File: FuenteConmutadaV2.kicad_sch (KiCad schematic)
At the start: 28 parts, among them J1 Conn_01x01_Pin, J2 Conn_01x01_Pin, J4 Conn_01x01_Pin, J5 USB_C_Receptacle_USB2.0

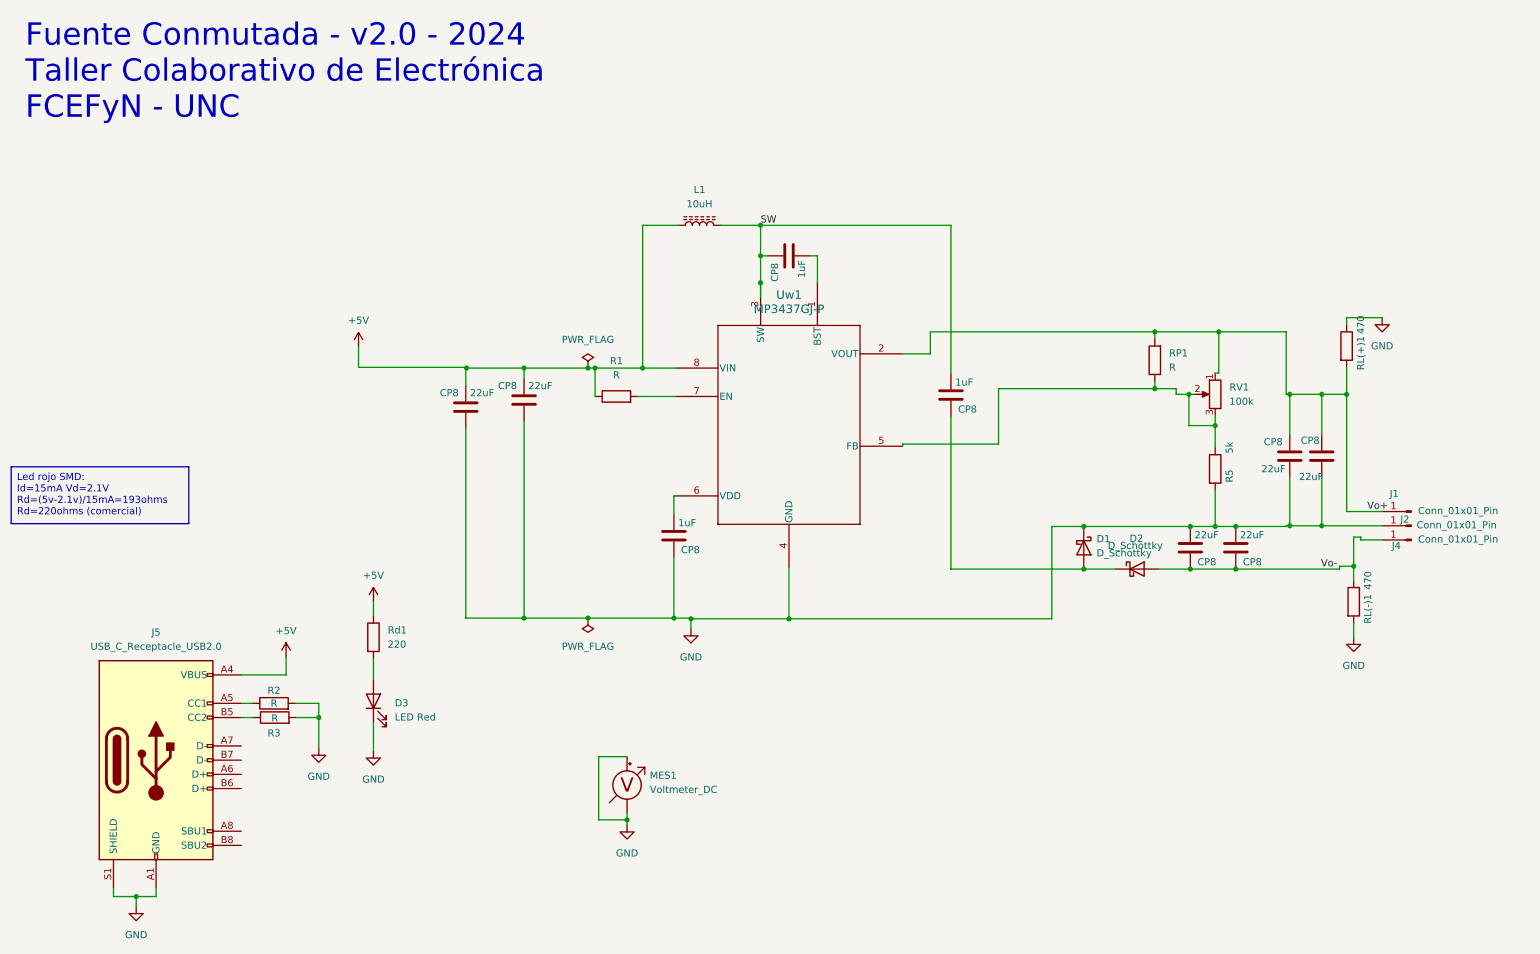
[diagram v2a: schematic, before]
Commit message: Cambios+pad banana
Pad banana diseñado
ajuste te tamaño de placa 80x40mm
ajuste vias
+mounting holes
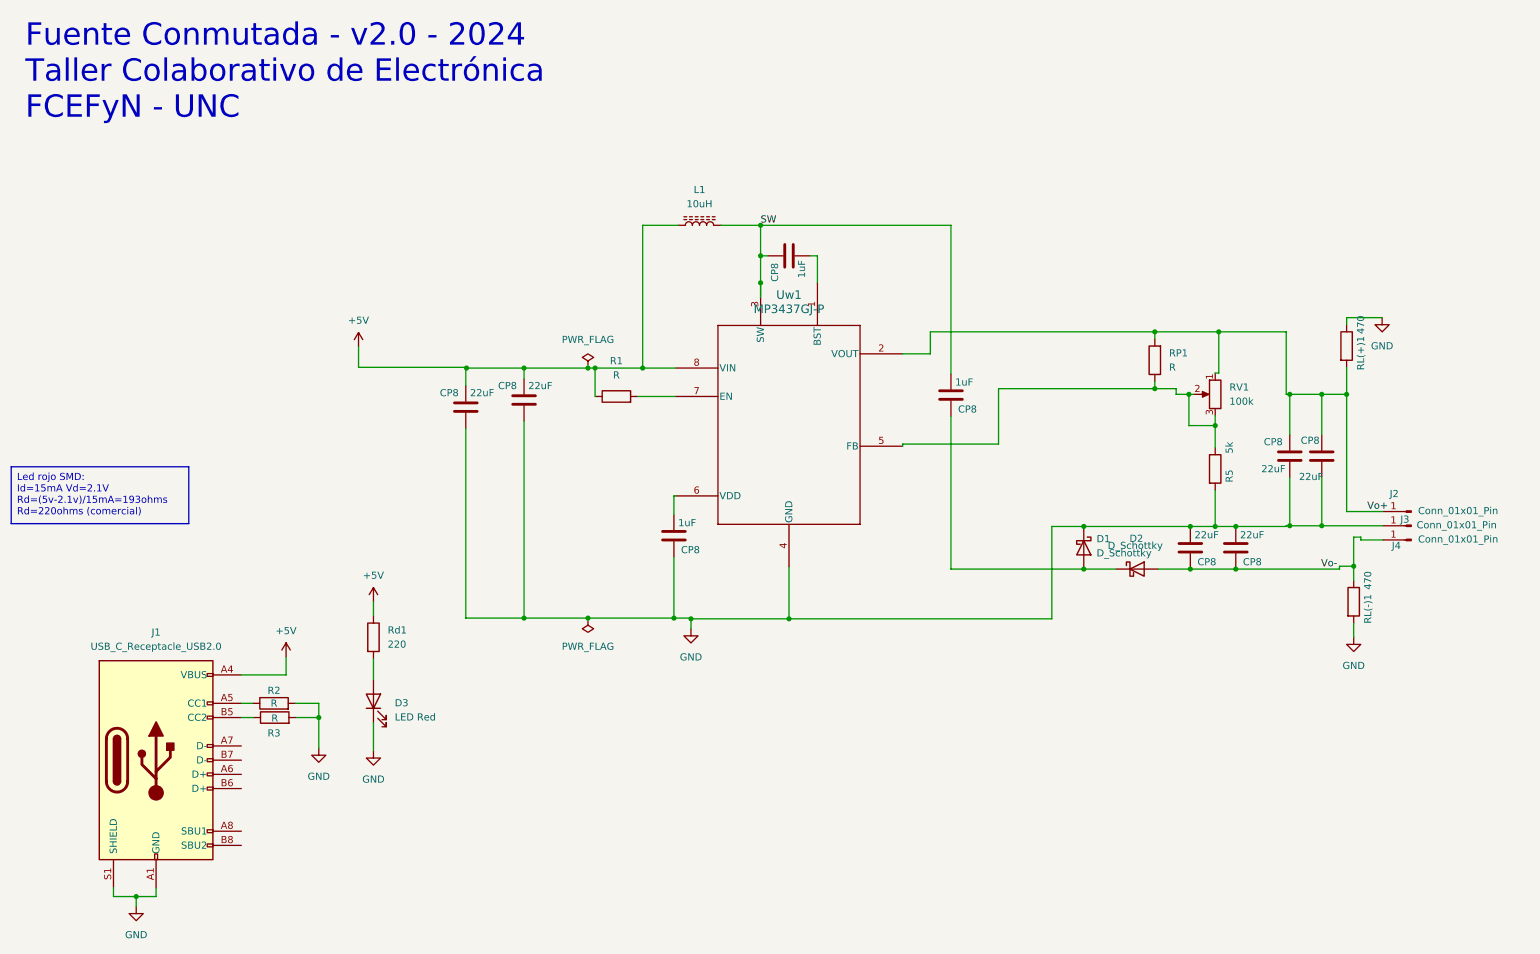
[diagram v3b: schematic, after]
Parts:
- removed MES1: Voltmeter_DC, Voltmeter:PRT-14313, symbol Device:Voltmeter_DC
- J2: renamed from J1; footprint Connector:CalTest_CT3151 -> Banana_elemon:Banana_209_elemon
- J3: renamed from J2; footprint Connector:CalTest_CT3151 -> Banana_elemon:Banana_209_elemon
- J4: footprint Connector:CalTest_CT3151 -> Banana_elemon:Banana_209_elemon
- renumbered J5 to J1
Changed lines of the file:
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@@
 	)
 	(junction
-		(at 124.079 159.639)
-		(diameter 0)
-		(color 0 0 0 0)
-	)
-	(junction
 		(at 95.377 78.867)
 		(diameter 0)
@@
 	(wire
 		(pts
-			(xy 124.079 148.336) (xy 118.999 148.336)
-		)
-		(stroke
-			(width 0)
-			(type default)
-		)
-	)
-	(wire
-		(pts
 			(xy 156.845 58.801) (xy 158.115 58.801)
 		)
@@
 	(wire
 		(pts
-			(xy 118.999 159.639) (xy 124.079 159.639)
-		)
-		(stroke
-			(width 0)
-			(type default)
-		)
-	)
-	(wire
-		(pts
 			(xy 78.74 120.65) (xy 78.74 123.19)
 		)
@@
 	(wire
 		(pts
-			(xy 124.079 159.639) (xy 124.079 160.528)
-		)
-		(stroke
-			(width 0)
-			(type default)
-		)
-	)
-	(wire
-		(pts
 			(xy 173.355 92.456) (xy 173.355 92.837)
 		)
@@
 	(wire
 		(pts
-			(xy 118.999 148.336) (xy 118.999 159.639)
-		)
-		(stroke
-			(width 0)
-			(type default)
-		)
-	)
-	(wire
-		(pts
 			(xy 229.235 89.154) (xy 229.235 93.091)
 		)
@@
 	(wire
 		(pts
-			(xy 124.079 158.496) (xy 124.079 159.639)
-		)
-		(stroke
-			(width 0)
-			(type default)
-		)
-	)
-	(wire
-		(pts
 			(xy 32.258 173.355) (xy 36.322 173.355)
 		)
@@
 	(symbol
 		(lib_id "power:GND")
-		(at 124.079 160.528 0)
-		(unit 1)
-		(exclude_from_sim no)
-		(in_bom yes)
-		(on_board yes)
-		(dnp no)
-		(fields_autoplaced yes)
-		(property "Reference" "#PWR06"
-			(at 124.079 166.878 0)
-			(effects
-				(font
-					(size 1.27 1.27)
-				)
-				(hide yes)
-			)
-		)
-		(property "Value" "GND"
-			(at 124.079 165.608 0)
-			(effects
-				(font
-					(size 1.27 1.27)
-				)
-			)
-		)
-		(property "Footprint" ""
-			(at 124.079 160.528 0)
-			(effects
-				(font
-					(size 1.27 1.27)
-				)
-				(hide yes)
-			)
-		)
-		(property "Datasheet" ""
-			(at 124.079 160.528 0)
-			(effects
-				(font
-					(size 1.27 1.27)
-				)
-				(hide yes)
-			)
-		)
-		(property "Description" ""
-			(at 124.079 160.528 0)
-			(effects
-				(font
-					(size 1.27 1.27)
-				)
-				(hide yes)
-			)
-		)
-		(pin "1"
-		)
-		(instances
-			(project "FuenteConmutadaV2"
-				(path "/d69a48d3-cc9a-476a-8449-ca4ce55f09c5"
-					(reference "#PWR06")
-					(unit 1)
-				)
-			)
-			(project "FuenteConmutada"
-				(path "/d7444c1b-87b0-4ff7-a57a-a32071ba4b64"
-					(reference "#PWR01")
-					(unit 1)
-				)
-			)
-		)
-	)
-	(symbol
-		(lib_id "power:GND")
 		(at 259.08 69.85 0)
 		(unit 1)
@@
 		(on_board yes)
 		(dnp no)
-		(property "Reference" "J2"
+		(property "Reference" "J3"
 			(at 263.144 105.918 0)
 			(effects
@@
 			)
 		)
-		(property "Footprint" "Connector:CalTest_CT3151"
-			(at 264.287 107.061 0)
+		(property "Footprint" "Banana_elemon:Banana_209_elemon"
+			(at 272.796 98.044 0)
 			(effects
 				(font
@@
 			(project "FuenteConmutadaV2"
 				(path "/d69a48d3-cc9a-476a-8449-ca4ce55f09c5"
-					(reference "J2")
+					(reference "J3")
 					(unit 1)
 				)
@@
 		(dnp no)
 		(fields_autoplaced yes)
-		(property "Reference" "J5"
+		(property "Reference" "J1"
 			(at 39.878 126.111 0)
 			(effects
@@
 			(project "FuenteConmutadaV2"
 				(path "/d69a48d3-cc9a-476a-8449-ca4ce55f09c5"
-					(reference "J5")
+					(reference "J1")
 					(unit 1)
 				)
@@
 		(on_board yes)
 		(dnp no)
-		(property "Reference" "J1"
+		(property "Reference" "J2"
 			(at 261.239 101.346 0)
 			(effects
@@
 			)
 		)
-		(property "Footprint" "Connector:CalTest_CT3151"
+		(property "Footprint" "Banana_elemon:Banana_209_elemon"
 			(at 264.287 104.521 0)
 			(effects
@@
 			(project "FuenteConmutadaV2"
 				(path "/d69a48d3-cc9a-476a-8449-ca4ce55f09c5"
-					(reference "J1")
+					(reference "J2")
 					(unit 1)
 				)
@@
 			)
 		)
-		(property "Footprint" "Connector:CalTest_CT3151"
+		(property "Footprint" "Banana_elemon:Banana_209_elemon"
 			(at 264.287 109.601 0)
 			(effects
@@
 					(unit 1)
 				)
-			)
-		)
-	)
-	(symbol
-		(lib_id "Device:Voltmeter_DC")
-		(at 124.079 153.416 0)
-		(unit 1)
-		(exclude_from_sim no)
-		(in_bom yes)
-		(on_board yes)
-		(dnp no)
-		(fields_autoplaced yes)
-		(property "Reference" "MES1"
-			(at 128.143 151.7015 0)
-			(effects
-				(font
-					(size 1.27 1.27)
-				)
-				(justify left)
-			)
-		)
-		(property "Value" "Voltmeter_DC"
-			(at 128.143 154.2415 0)
-			(effects
-				(font
-					(size 1.27 1.27)
-				)
-				(justify left)
-			)
-		)
-		(property "Footprint" "Voltmeter:PRT-14313"
-			(at 124.079 150.876 90)
-			(effects
-				(font
-					(size 1.27 1.27)
-				)
-				(hide yes)
-			)
-		)
-		(property "Datasheet" "~"
-			(at 124.079 150.876 90)
-			(effects
-				(font
-					(size 1.27 1.27)
-				)
-				(hide yes)
-			)
-		)
-		(property "Description" ""
-			(at 124.079 153.416 0)
-			(effects
-				(font
-					(size 1.27 1.27)
-				)
-				(hide yes)
-			)
-		)
-		(pin "1"
-		)
-		(pin "2"
-		)
-		(instances
-			(project "FuenteConmutadaV2"
-				(path "/d69a48d3-cc9a-476a-8449-ca4ce55f09c5"
-					(reference "MES1")
-					(unit 1)
-				)

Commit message: Cambios
+pote
 +conectores banana
 +usb_c
+pads, footprints & 3dmodels
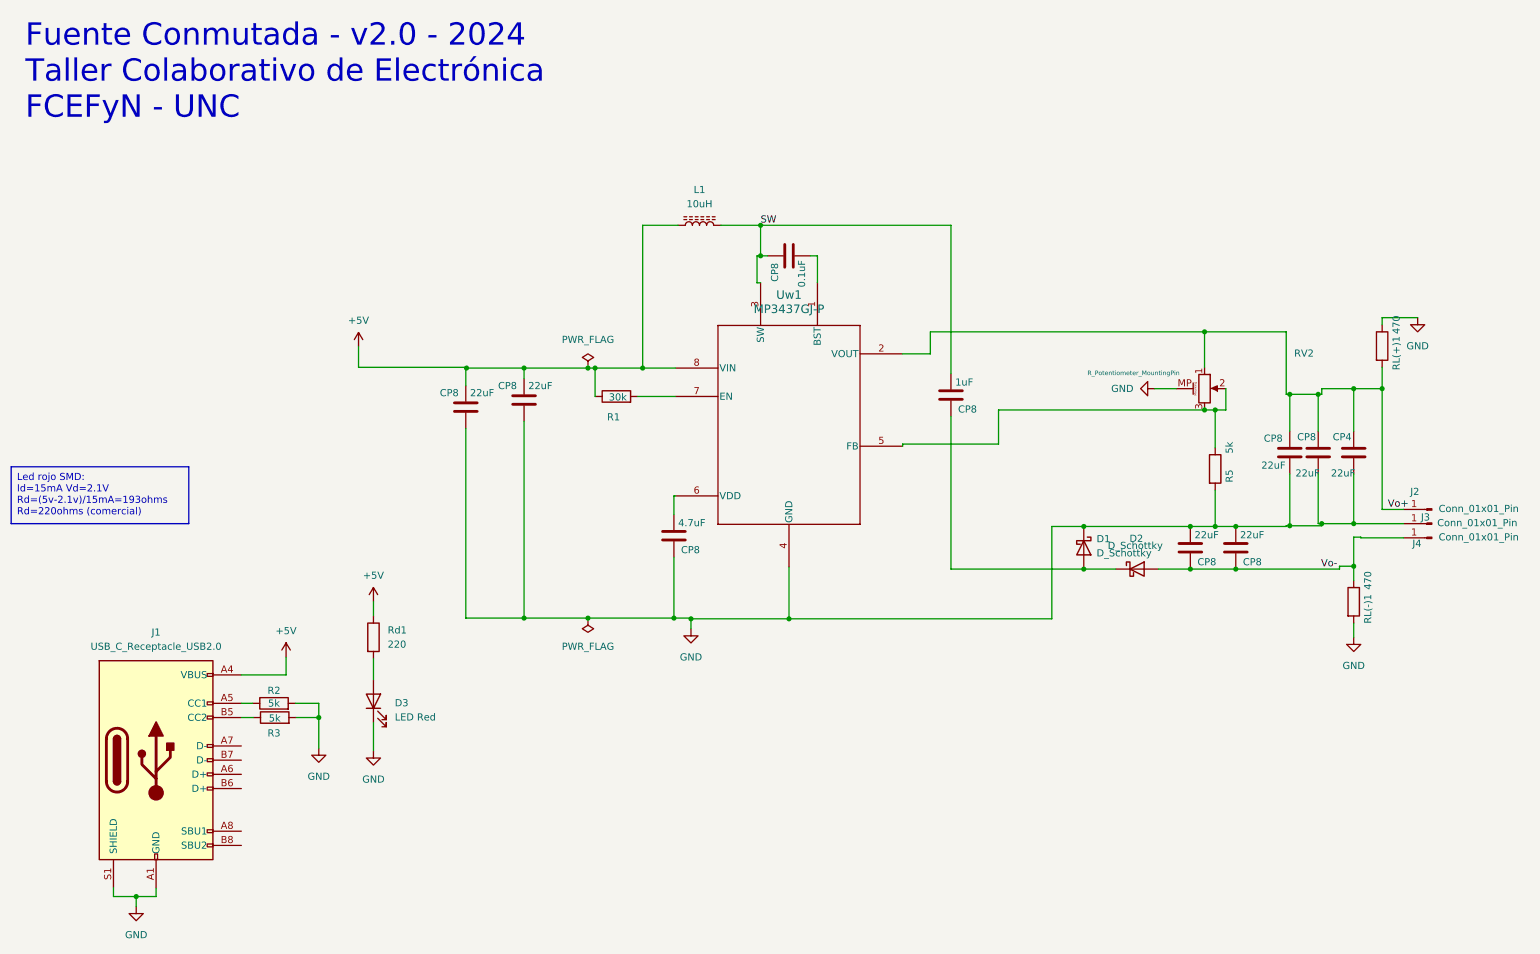
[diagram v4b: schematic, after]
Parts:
- removed RP1: R, Resistor_SMD:R_1206_3216Metric_Pad1.30x1.75mm_HandSolder, symbol Device:R
- removed RV1: 100k, Potentiometer_THT:Potentiometer_Alps_RK163_Single_Horizontal, symbol Device:R_Potentiometer
- added CP4: 22uF, Capacitor_SMD:C_1206_3216Metric_Pad1.33x1.80mm_HandSolder, symbol Device:C
- added RV2: R_Potentiometer_MountingPin, Pote:PDB12M4251105BF, symbol Device:R_Potentiometer_MountingPin
- CP8: value 1uF -> 0.1uF
- CP8: value 1uF -> 4.7uF
- J1: footprint Connector_USB:USB_C_Receptacle_GCT_USB4105-xx-A_16P_TopMnt_Horizontal -> USB_Amphenol:AMPHENOL_10164359-00011LF
- J2, J3, J4: footprint Banana_elemon:Banana_209_elemon -> Banana_CT:Banana_CT_6mm
- R1: value R -> 30k
- R2, R3: value R -> 5k
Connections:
- net GND: now also CP4.1, RV2.MP (MountPin)
- net Vo+: now also CP4.2, RV2.1
- net at R5.1, Uw1.5 (FB): now also RV2.2, RV2.3
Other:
- moved on the sheet: CP8, J2, J3, J4, RL(+)1
